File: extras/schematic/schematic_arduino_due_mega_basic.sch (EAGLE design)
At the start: 20 parts, among them U1 SI4735-D60-GU

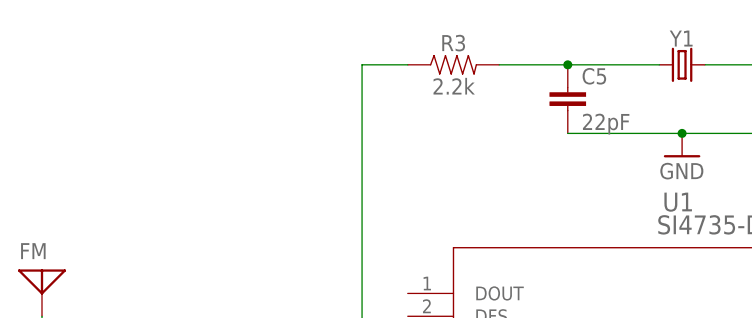
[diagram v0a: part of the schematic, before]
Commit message: SI473X Arduino Library
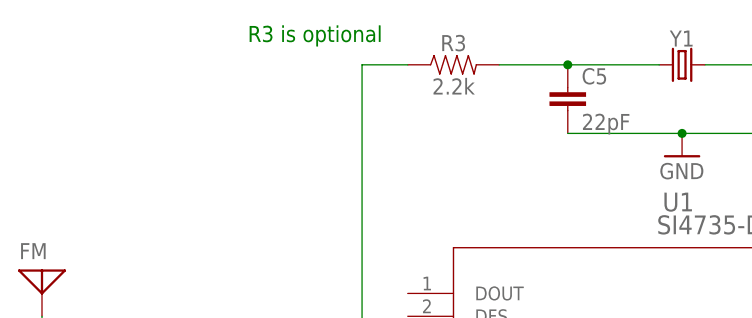
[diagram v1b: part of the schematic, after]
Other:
- note added: "R3 is optional"
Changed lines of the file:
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@@
 <text x="12.7" y="68.58" size="1.778" layer="91">If GND, I2C addr =  0x11</text>
 <text x="12.7" y="63.5" size="1.778" layer="91">If VCC, I2C addr =  0x63</text>
+<text x="-50.8" y="157.48" size="1.778" layer="91">R3 is optional</text>
+<rectangle x1="-33.02" y1="149.86" x2="-22.86" y2="160.02" layer="205"/>
 </plain>
 <instances>
